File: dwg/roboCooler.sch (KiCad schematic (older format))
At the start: 54 parts, among them J1 CONN_01X02, J10 CONN_01X04, J11 CONN_01X04, J12 USB_A, J13 CONN_02X03, J14 CONN_02X03, J2 CONN_01X02, J3 Discovery_F407_P1, J4 CONN_01X06, J5 CONN_01X12, J6 Discovery_F407_P2, J7 CONN_02X03, J8 CONN_01X02, J9 CONN_01X02, Q1 NMOS, Q2 NMOS, SW1 SPST_4PIN, SW2 SPST_4PIN, U1 SN74LV, U2 TB6549

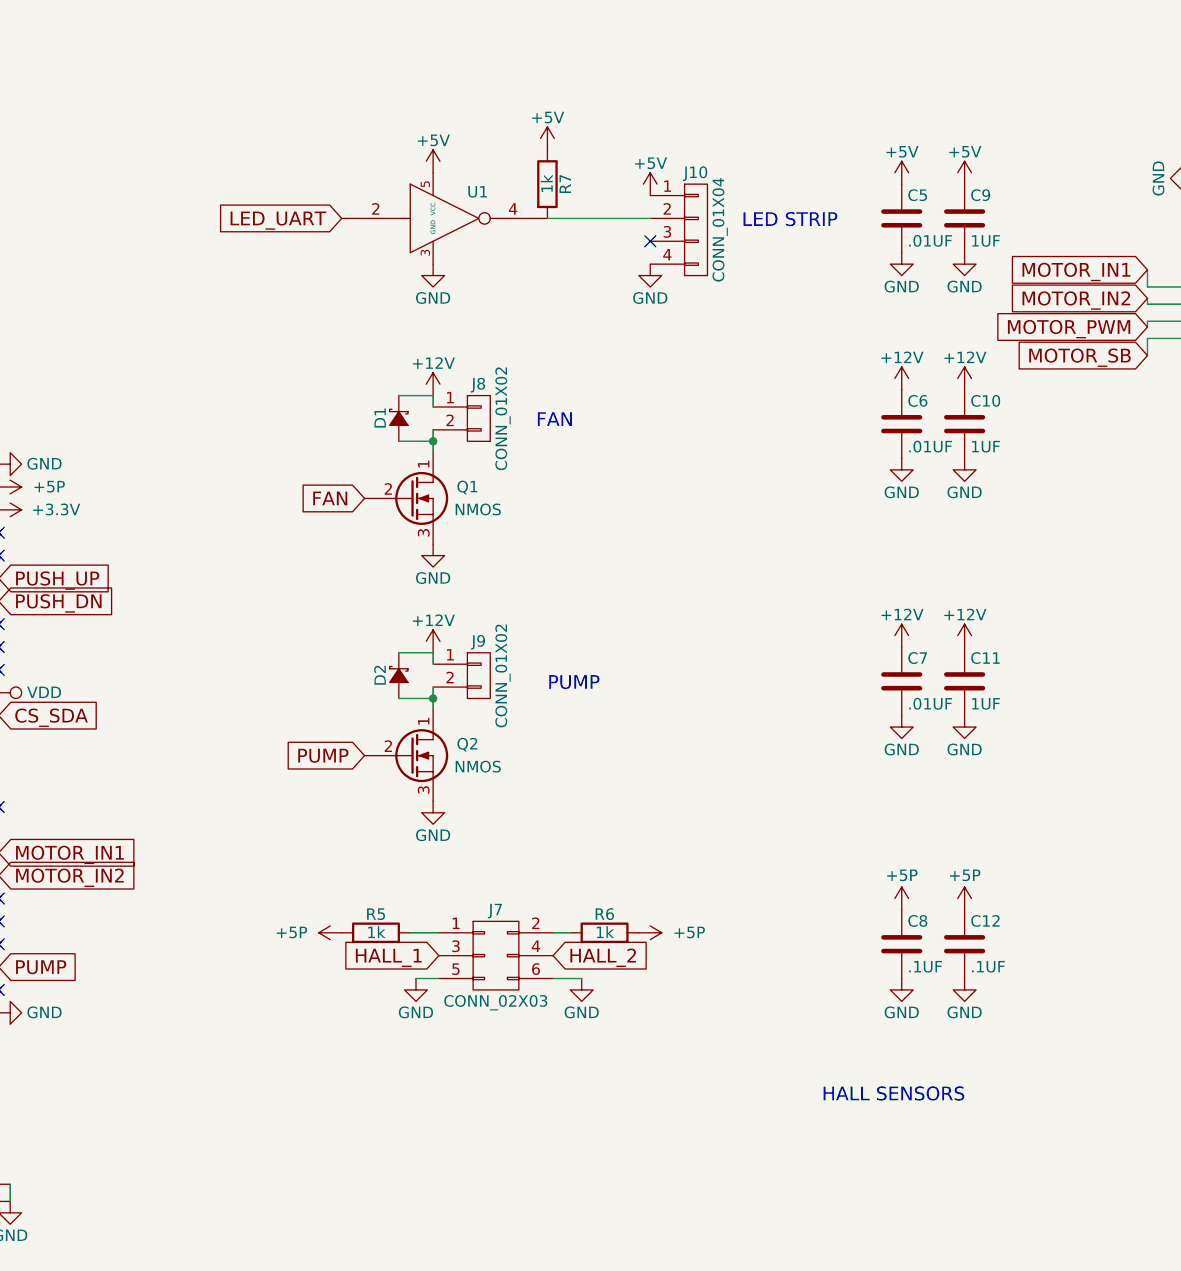
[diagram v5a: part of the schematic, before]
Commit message: moved led fan and pump to 6-pin conns
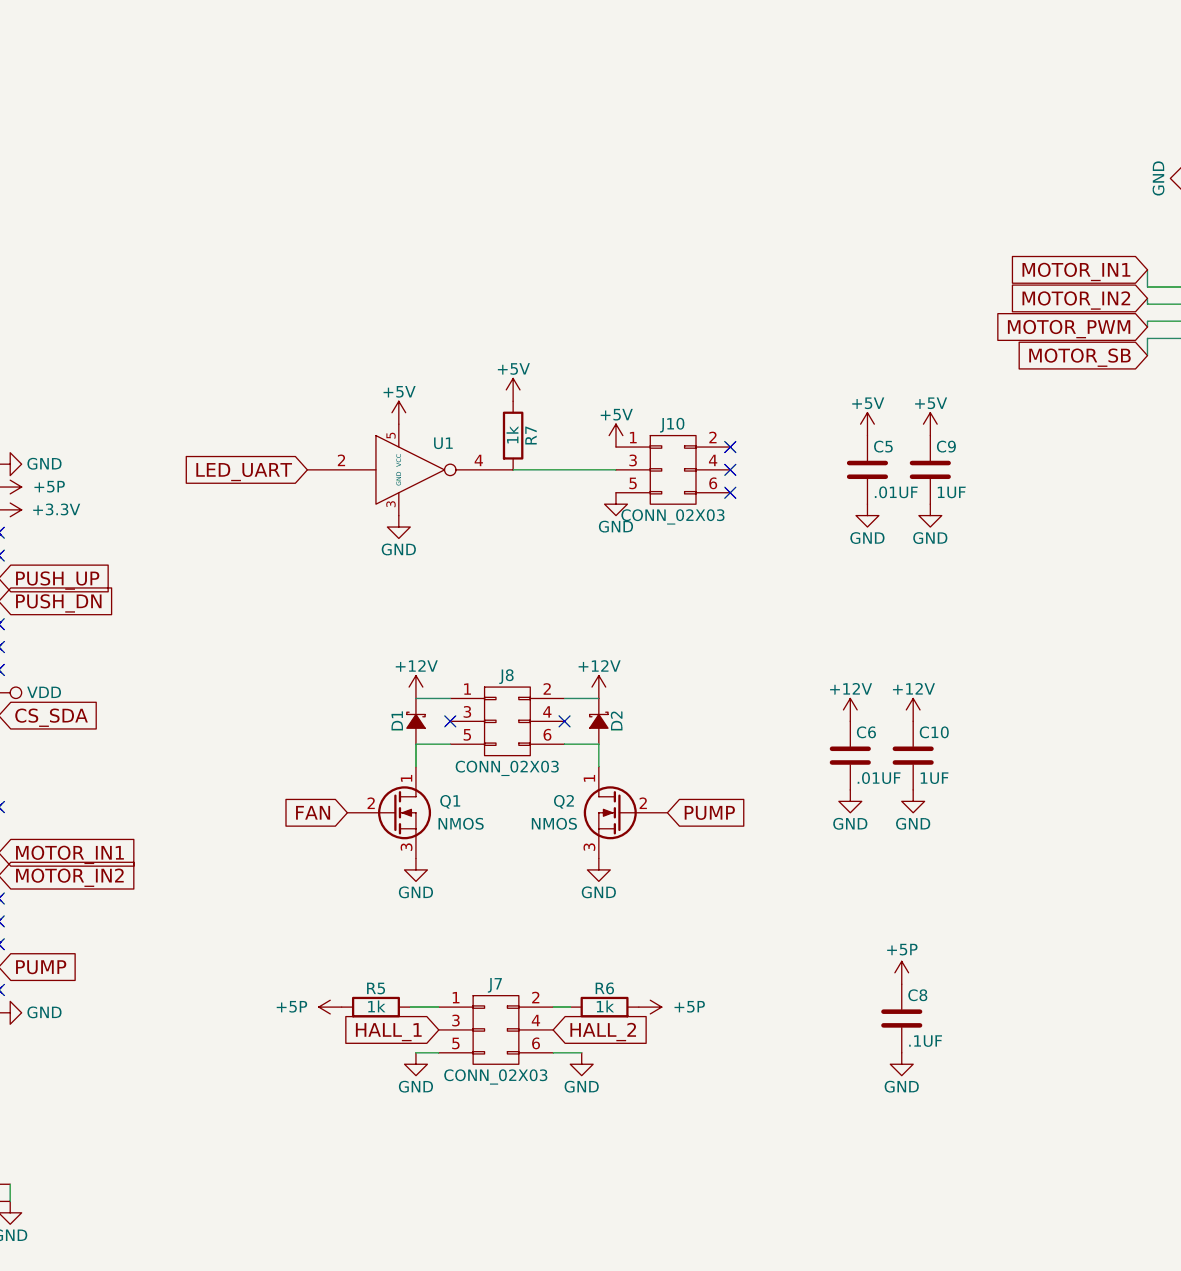
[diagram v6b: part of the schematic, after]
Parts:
- removed C11: 1UF, Capacitors_SMD:C_0805_HandSoldering, symbol C
- removed C12: .1UF, Capacitors_SMD:C_0805_HandSoldering, symbol C
- removed C7: .01UF, Capacitors_SMD:C_0805_HandSoldering, symbol C
- removed J10: CONN_01X04, Socket_Strips:Socket_Strip_Angled_1x04, symbol CONN_01X04
- removed J8, J9: CONN_01X02, Socket_Strips:Socket_Strip_Angled_1x02, symbol CONN_01X02
- added J10, J8: CONN_02X03, Pin_Headers:Pin_Header_Angled_2x03, symbol CONN_02X03
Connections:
- net +12V: now also J8.1 (P1), J8.2 (P2)
- net +5V: now also J10.1 (P1)
- net GND: now also J10.5 (P5)
- net at D1.2 (A), Q1.1 (D): now also J8.5 (P5)
- net at R7.2, U1.4: now also J10.3 (P3)
- net at D2.2 (A), Q2.1 (D): now also J8.6 (P6)
- no-connect marks 33 -> 37
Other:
- note removed: "FAN"
- note removed: "HALL SENSORS"
- note removed: "LED STRIP"
- note removed: "PUMP"
- moved on the sheet: C10, C5, C6, C8, C9, D1, J7, Q1, R5, R6, R7, U1

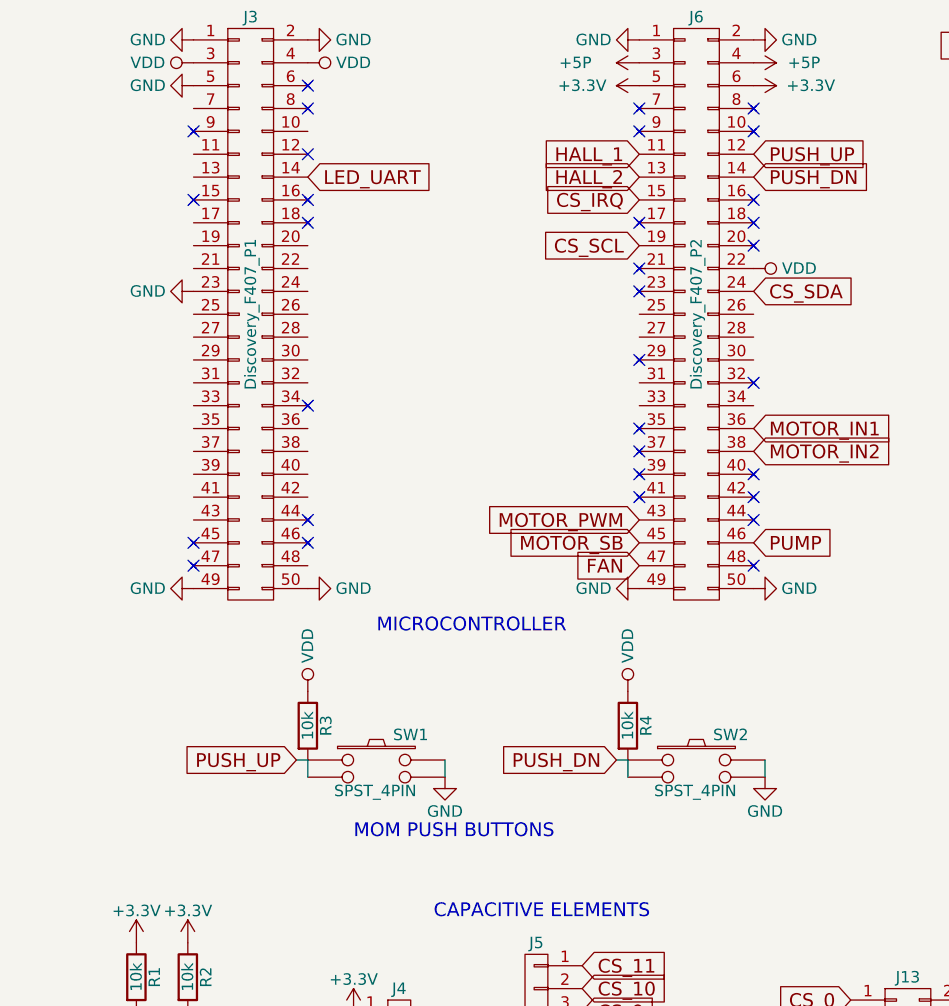
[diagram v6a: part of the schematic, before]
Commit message: moved all components inside the disc envelope
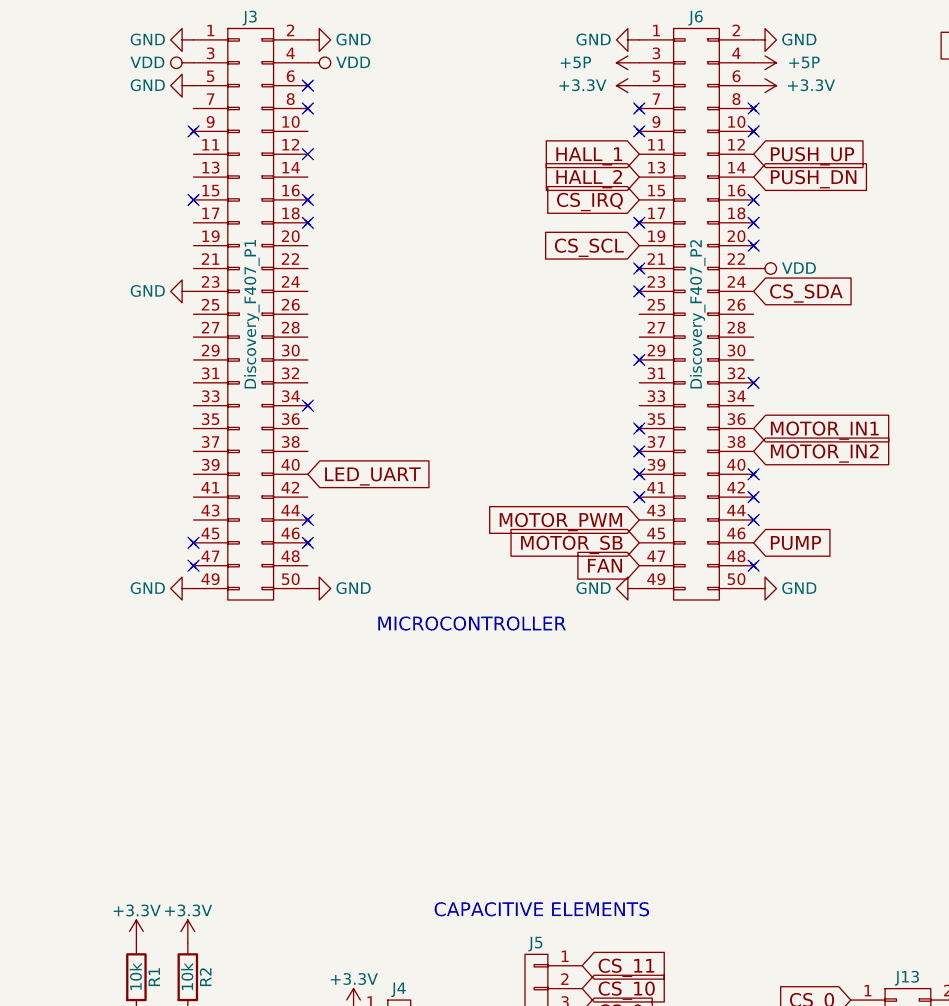
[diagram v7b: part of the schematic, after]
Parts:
- removed R3, R4: 10k, Resistors_SMD:R_0805_HandSoldering, symbol R
- removed SW1, SW2: SPST_4PIN, roboCooler:D6C90, symbol SPST_4PIN
- J1, J2: footprint Pin_Headers:Pin_Header_Angled_1x02 -> roboCooler:Pin_Header_Angled_1x02_200mil
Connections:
- net LED_UART: now also J3.40 (P40); no longer J3.14 (P14)
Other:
- note removed: "MOM PUSH BUTTONS"
